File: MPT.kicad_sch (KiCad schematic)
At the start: 0 parts

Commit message: Mountingholes Added
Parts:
- added H1, H2, H3, H4: MountingHole, MountingHole:MountingHole_2.2mm_M2, symbol Mechanical:MountingHole
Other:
- note added: "ToDos: - Testpoints - IC LED Treiber neu - Routing (Nico)"
- note removed: "ToDos: - Mounting Holes - Maybe a Buzzer (Probably not) - Testpoints"

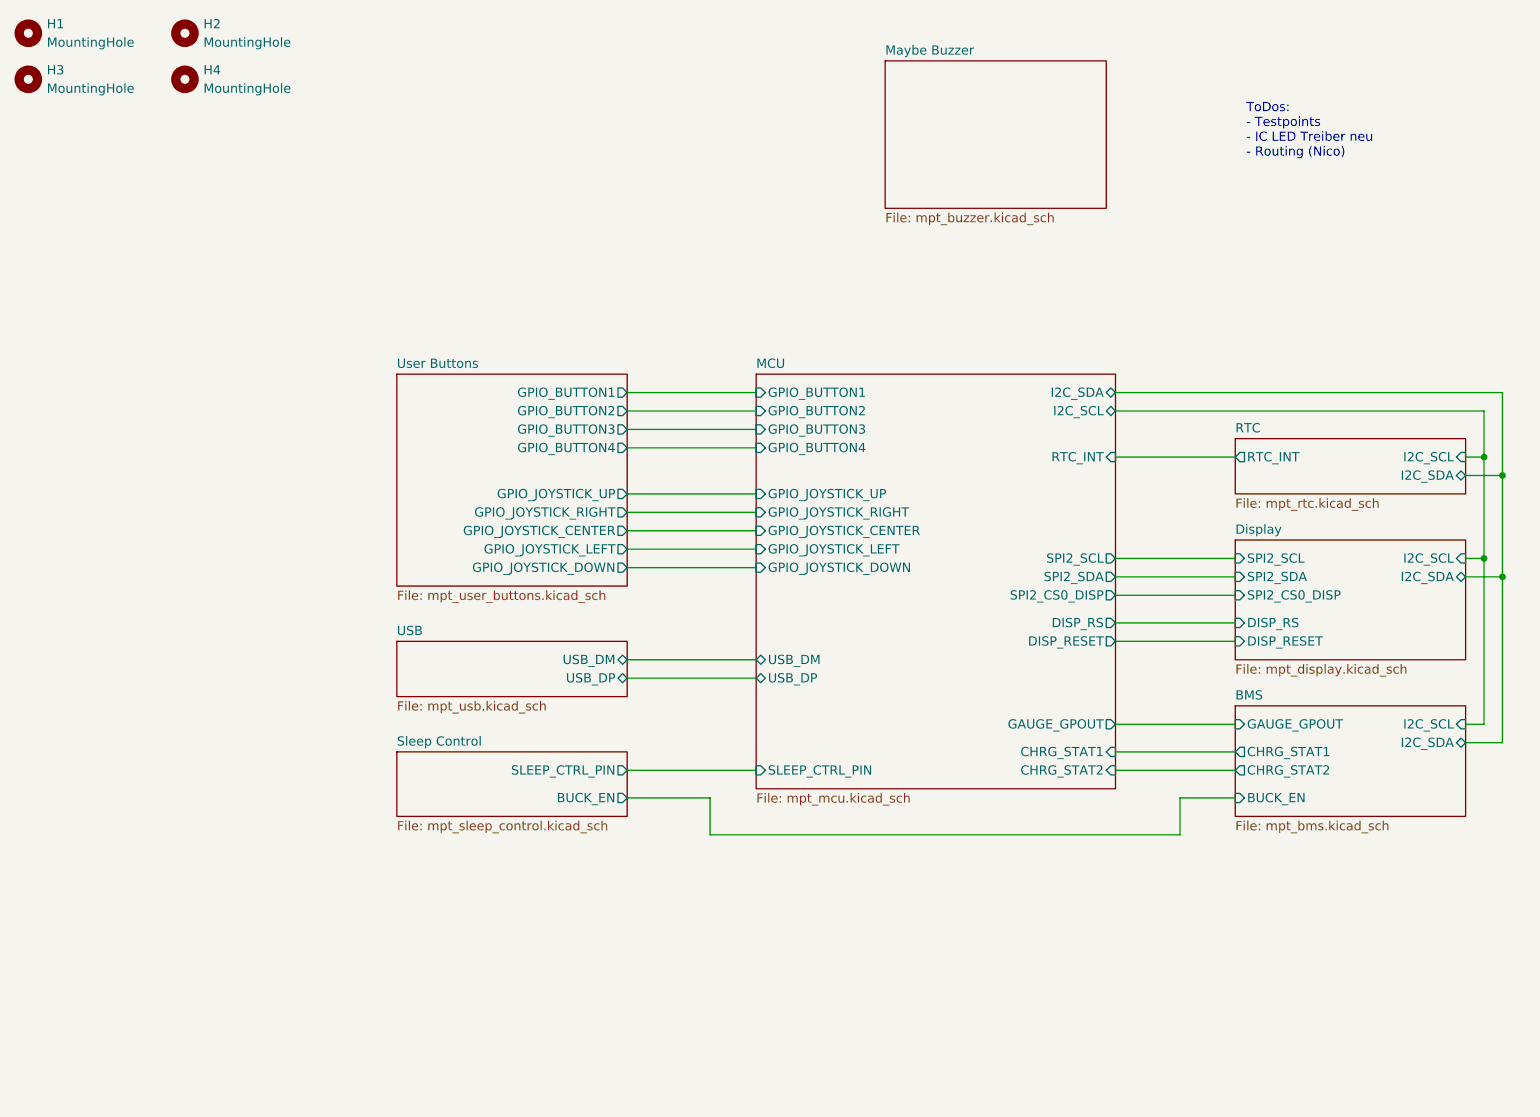
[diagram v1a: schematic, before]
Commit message: Replace LED Driver Remove maybe buzzer
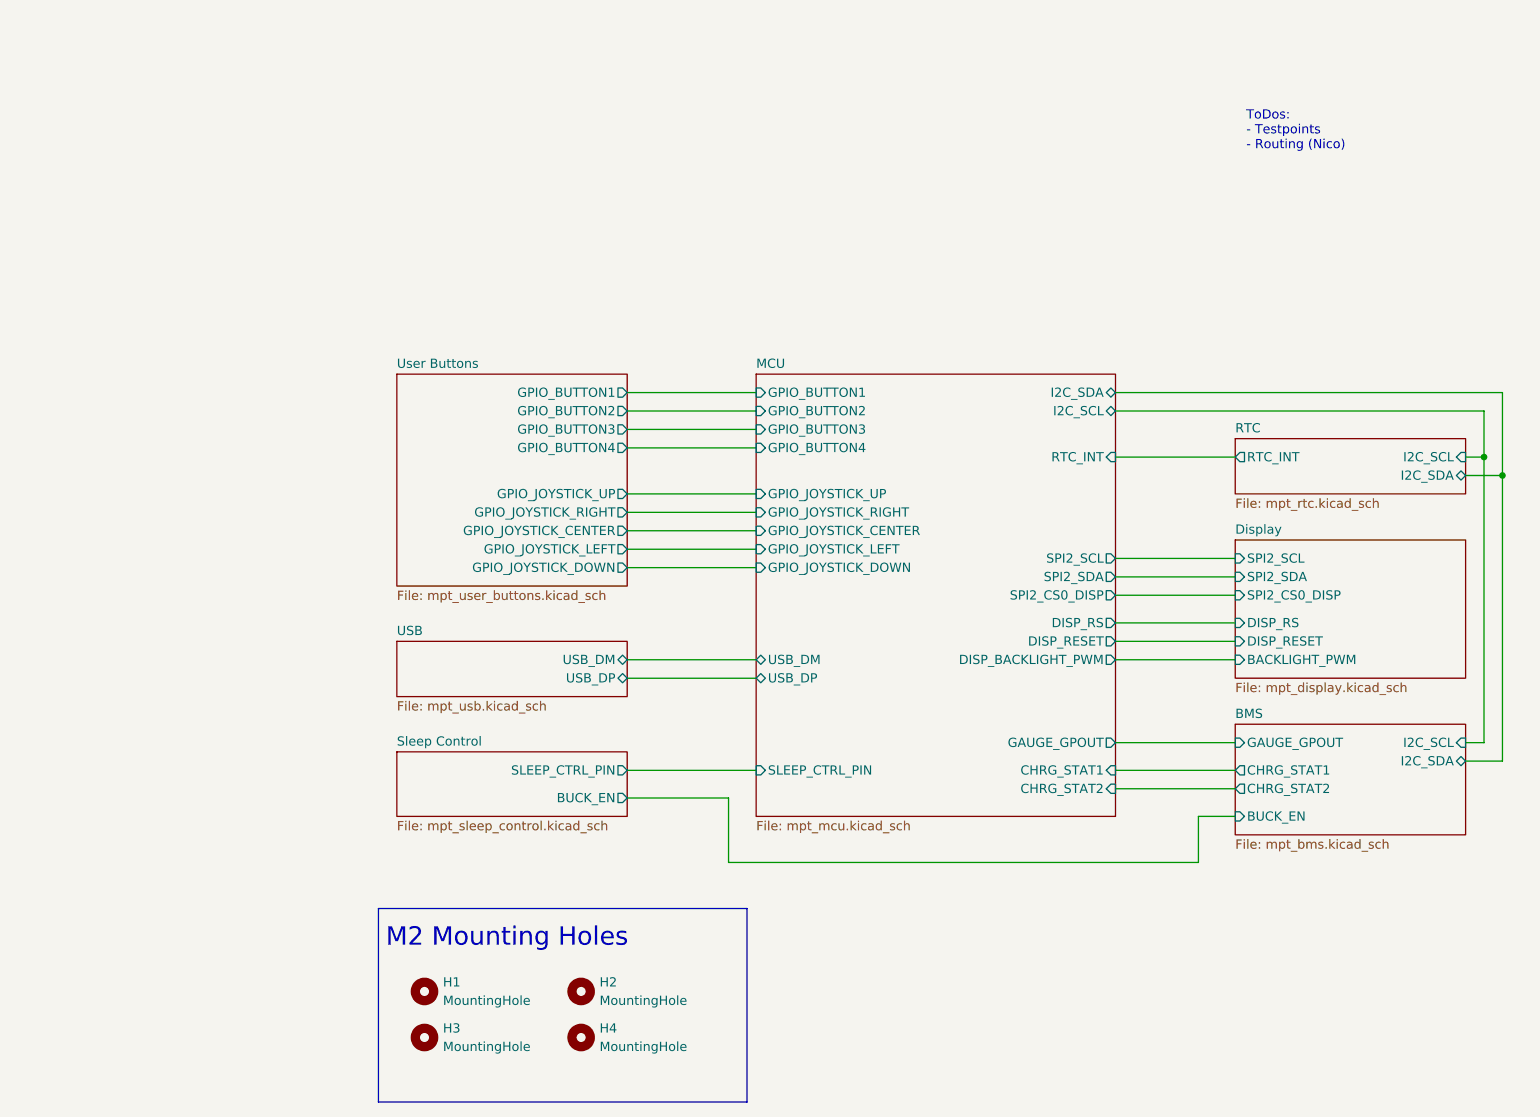
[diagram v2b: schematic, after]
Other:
- removed sheet Maybe Buzzer
- sheet Display ports: added BACKLIGHT_PWM; removed I2C_SCL, I2C_SDA
- sheet MCU ports: added DISP_BACKLIGHT_PWM; removed none
- note added: "M2 Mounting Holes"
- note added: "ToDos: - Testpoints - Routing (Nico)"
- note removed: "ToDos: - Testpoints - IC LED Treiber neu - Routing (Nico)"
- moved on the sheet: H1, H2, H3, H4
